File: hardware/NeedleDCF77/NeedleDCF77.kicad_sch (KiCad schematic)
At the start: 84 parts, among them J1 USB_C_Receptacle_USB2.0, J2 Battery, J3 DSW, J4 UART, J5 Hours, J6 Minutes, J7 Seconds, Q1 AO3401A, Q2 AO3400A, SW1 ShowDate, U1 LTC3558, U2 STM32L051C8Tx, U3 MAS6180_77kHz, U4 LT1617, U5 PT6312, U6 LM4871, Y2 32.768kHz

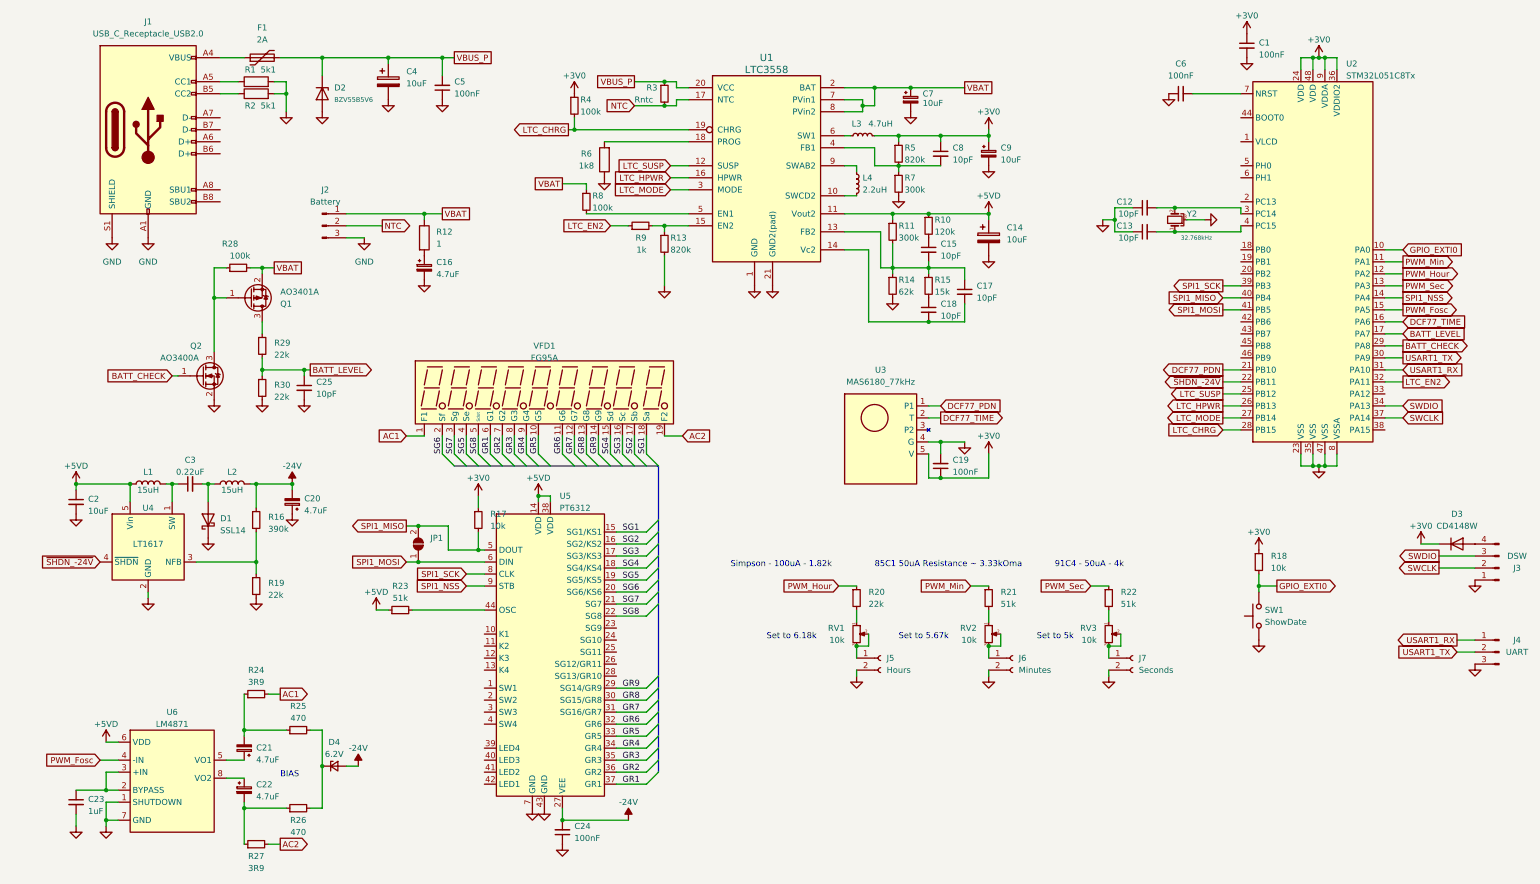
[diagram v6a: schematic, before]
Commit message: Initial version of PCB placement and routing
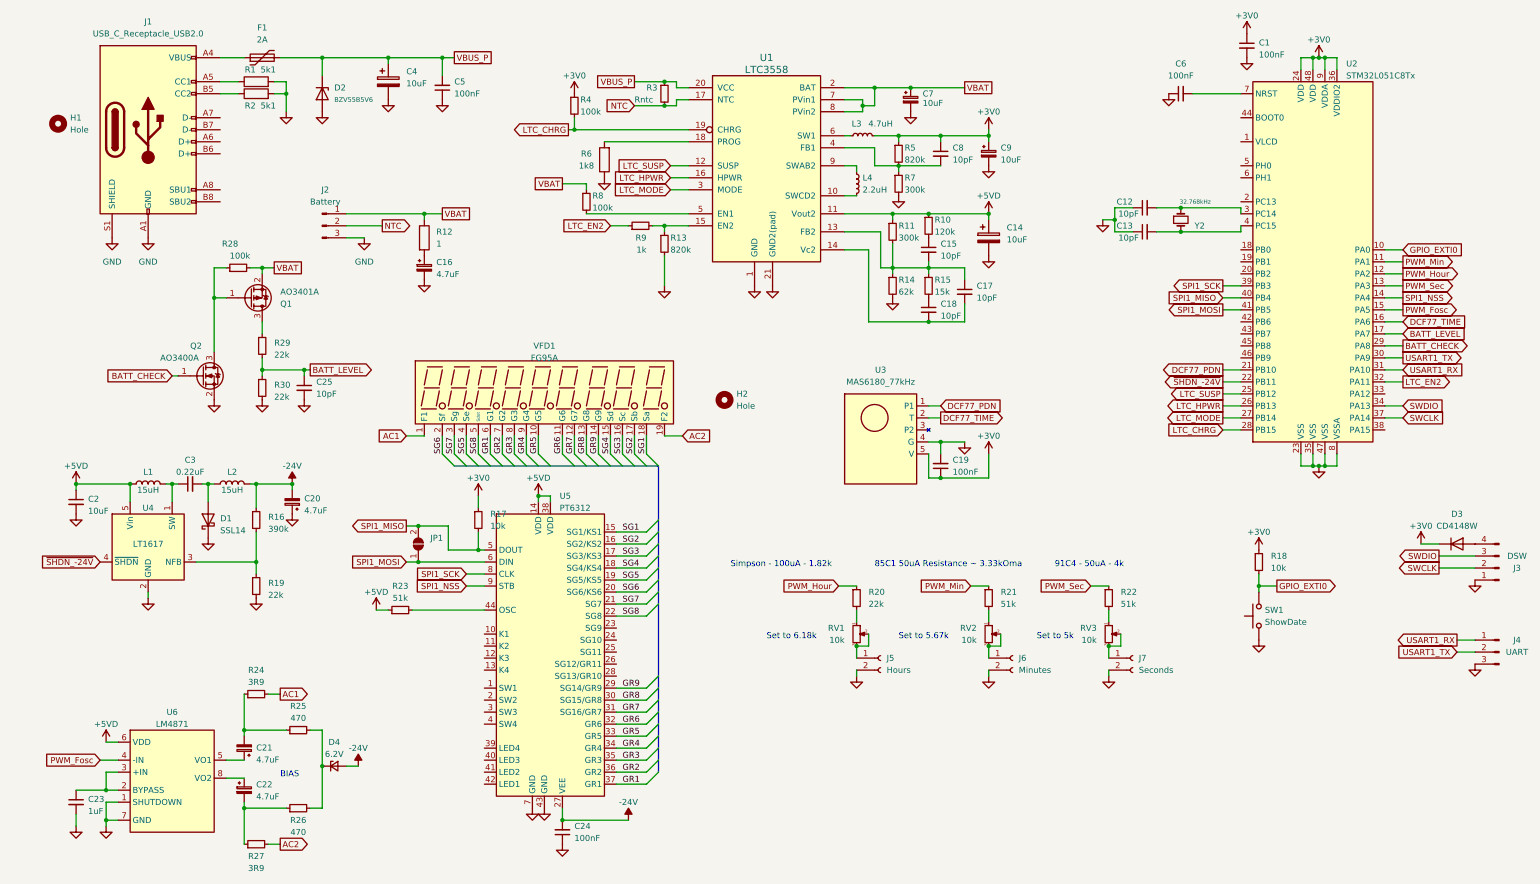
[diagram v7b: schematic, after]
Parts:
- added H1, H2: Hole, MountingHole:MountingHole_3.2mm_M3_DIN965_Pad_TopBottom, symbol Mechanical:MountingHole
- J1: footprint Connector_USB:USB_C_Receptacle_HRO_TYPE-C-31-M-12 -> Molex USB C:Molex-2169890001-MFG; Alie TYPE-C-31-M-12 -> 2169890001
- Y2: footprint Crystal:Crystal_C38-LF_D3.0mm_L8.0mm_Horizontal_1EP_style2 -> Crystal:Crystal_C38-LF_D3.0mm_L8.0mm_Horizontal; symbol Device:Crystal_GND3_Small -> Device:Crystal_Small
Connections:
- net GND: no longer Y2.3
- net at C13.2, U2.4 (PC15): now also Y2.2; no longer Y2.1
- net at C12.2, U2.3 (PC14): now also Y2.1; no longer Y2.2
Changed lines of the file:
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@@
   (junction (at 195.58 71.12) (diameter 0) (color 0 0 0 0)
   )
+  (junction (at 256.54 63.5) (diameter 0) (color 0 0 0 0)
+  )
   (junction (at 68.58 116.84) (diameter 0) (color 0 0 0 0)
   )
@@
   (junction (at 241.3 151.13) (diameter 0) (color 0 0 0 0)
   )
-  (junction (at 255.27 63.5) (diameter 0) (color 0 0 0 0)
-  )
   (junction (at 205.74 115.57) (diameter 0) (color 0 0 0 0)
   )
   (junction (at 205.74 43.18) (diameter 0) (color 0 0 0 0)
   )
+  (junction (at 256.54 58.42) (diameter 0) (color 0 0 0 0)
+  )
   (junction (at 60.96 116.84) (diameter 0) (color 0 0 0 0)
   )
   (junction (at 242.57 60.96) (diameter 0) (color 0 0 0 0)
   )
-  (junction (at 255.27 58.42) (diameter 0) (color 0 0 0 0)
-  )
   (junction (at 95.25 125.73) (diameter 0) (color 0 0 0 0)
   )
@@
     (stroke (width 0) (type default))
   )
-  (wire (pts (xy 251.46 63.5) (xy 255.27 63.5))
-    (stroke (width 0) (type default))
-  )
   (wire (pts (xy 241.3 156.21) (xy 241.3 157.48))
     (stroke (width 0) (type default))
@@
     (stroke (width 0) (type default))
   )
-  (wire (pts (xy 251.46 58.42) (xy 255.27 58.42))
-    (stroke (width 0) (type default))
-  )
   (bus (pts (xy 146.05 170.18) (xy 146.05 172.72))
     (stroke (width 0) (type default))
@@
     (stroke (width 0) (type default))
   )
-  (wire (pts (xy 255.27 58.42) (xy 269.24 58.42))
+  (wire (pts (xy 251.46 58.42) (xy 256.54 58.42))
     (stroke (width 0) (type default))
   )
@@
     (stroke (width 0) (type default))
   )
-  (wire (pts (xy 255.27 63.5) (xy 269.24 63.5))
+  (wire (pts (xy 251.46 63.5) (xy 256.54 63.5))
     (stroke (width 0) (type default))
   )
@@
     (stroke (width 0) (type default))
   )
-  (wire (pts (xy 257.81 60.96) (xy 261.62 60.96))
-    (stroke (width 0) (type default))
-  )
   (bus (pts (xy 146.05 165.1) (xy 146.05 167.64))
     (stroke (width 0) (type default))
@@
     (stroke (width 0) (type default))
   )
+  (wire (pts (xy 256.54 63.5) (xy 269.24 63.5))
+    (stroke (width 0) (type default))
+  )
   (wire (pts (xy 137.16 175.26) (xy 143.51 175.26))
     (stroke (width 0) (type default))
@@
     (stroke (width 0) (type default))
   )
+  (wire (pts (xy 256.54 58.42) (xy 269.24 58.42))
+    (stroke (width 0) (type default))
+  )
   (text "91C4 - 50uA - 4k" (at 229.87 134.62 0)
     (effects (font (size 1.27 1.27)) (justify left bottom))
@@
       (effects (font (size 1.27 1.27)))
     )
-    (property "Footprint" "Connector_USB:USB_C_Receptacle_HRO_TYPE-C-31-M-12" (at 41.91 41.91 0)
+    (property "Footprint" "Molex USB C:Molex-2169890001-MFG" (at 41.91 41.91 0)
       (effects (font (size 1.27 1.27)) hide)
     )
-    (property "Datasheet" "https://www.usb.org/sites/default/files/documents/usb_type-c.zip" (at 41.91 41.91 0)
+    (property "Datasheet" "https://www.molex.com/content/dam/molex/molex-dot-com/products/automated/en-us/salesdrawingpdf/216/216989/2169890001_sd.pdf?inline" (at 41.91 41.91 0)
       (effects (font (size 1.27 1.27)) hide)
     )
-    (property "Alie" "TYPE-C-31-M-12" (at 38.1 41.91 0)
+    (property "Alie" "2169890001" (at 38.1 41.91 0)
       (effects (font (size 1.27 1.27)) hide)
     )
@@
     )
   )
+  (symbol (lib_id "Mechanical:MountingHole") (at 19.05 40.64 0) (unit 1)
+    (in_bom yes) (on_board yes) (dnp no) (fields_autoplaced)
+    (property "Reference" "H1" (at 21.59 39.37 0)
+      (effects (font (size 1.27 1.27)) (justify left))
+    )
+    (property "Value" "Hole" (at 21.59 41.91 0)
+      (effects (font (size 1.27 1.27)) (justify left))
+    )
+    (property "Footprint" "MountingHole:MountingHole_3.2mm_M3_DIN965_Pad_TopBottom" (at 19.05 40.64 0)
+      (effects (font (size 1.27 1.27)) hide)
+    )
+    (property "Datasheet" "~" (at 19.05 40.64 0)
+      (effects (font (size 1.27 1.27)) hide)
+    )
+    (property "Kelco" "#8282" (at 19.05 40.64 0)
+      (effects (font (size 1.27 1.27)) hide)
+    )
+    (instances
+      (project "NeedleDCF77"
+        (path "/9538e4ed-27e6-4c37-b989-9859dc0d49e8"
+          (reference "H1") (unit 1)
+        )
+      )
+    )
+  )
   (symbol (lib_id "Device:R_Small") (at 62.23 87.63 0) (unit 1)
     (in_bom yes) (on_board yes) (dnp no) (fields_autoplaced)
@@
     )
   )
-  (symbol (lib_id "Device:Crystal_GND3_Small") (at 255.27 60.96 90) (unit 1)
+  (symbol (lib_id "Device:Crystal_Small") (at 256.54 60.96 270) (unit 1)
     (in_bom yes) (on_board yes) (dnp no)
-    (property "Reference" "Y2" (at 257.81 59.6899 90)
+    (property "Reference" "Y2" (at 261.62 62.23 90)
       (effects (font (size 1.27 1.27)) (justify right))
     )
-    (property "Value" "32.768kHz" (at 256.54 64.77 90)
+    (property "Value" "32.768kHz" (at 262.89 57.15 90)
       (effects (font (size 0.9 0.9)) (justify right))
     )
-    (property "Footprint" "Crystal:Crystal_C38-LF_D3.0mm_L8.0mm_Horizontal_1EP_style2" (at 255.27 60.96 0)
+    (property "Footprint" "Crystal:Crystal_C38-LF_D3.0mm_L8.0mm_Horizontal" (at 256.54 60.96 0)
       (effects (font (size 1.27 1.27)) hide)
     )
-    (property "Datasheet" "~" (at 255.27 60.96 0)
+    (property "Datasheet" "~" (at 256.54 60.96 0)
       (effects (font (size 1.27 1.27)) hide)
     )
-    (property "Kelco" "#13076" (at 255.27 60.96 90)
+    (property "Kelco" "#13076" (at 256.54 60.96 90)
       (effects (font (size 1.27 1.27)) hide)
     )
     (pin "1")
     (pin "2")
-    (pin "3")
     (instances
       (project "NeedleDCF77"
@@
     )
   )
+  (symbol (lib_id "Mechanical:MountingHole") (at 160.02 99.06 0) (unit 1)
+    (in_bom yes) (on_board yes) (dnp no) (fields_autoplaced)
+    (property "Reference" "H2" (at 162.56 97.79 0)
+      (effects (font (size 1.27 1.27)) (justify left))
+    )
+    (property "Value" "Hole" (at 162.56 100.33 0)
+      (effects (font (size 1.27 1.27)) (justify left))
+    )
+    (property "Footprint" "MountingHole:MountingHole_3.2mm_M3_DIN965_Pad_TopBottom" (at 160.02 99.06 0)
+      (effects (font (size 1.27 1.27)) hide)
+    )
+    (property "Datasheet" "~" (at 160.02 99.06 0)
+      (effects (font (size 1.27 1.27)) hide)
+    )
+    (property "Kelco" "#8282" (at 160.02 99.06 0)
+      (effects (font (size 1.27 1.27)) hide)
+    )
+    (instances
+      (project "NeedleDCF77"
+        (path "/9538e4ed-27e6-4c37-b989-9859dc0d49e8"
+          (reference "H2") (unit 1)
+        )
+      )
+    )
+  )
   (symbol (lib_id "Transistor_FET:AO3401A") (at 59.69 77.47 0) (mirror x) (unit 1)
     (in_bom yes) (on_board yes) (dnp no)
@@
         )
       )
-    )
-  )
-  (symbol (lib_id "power:GND") (at 261.62 60.96 90) (unit 1)
-    (in_bom yes) (on_board yes) (dnp no) (fields_autoplaced)
-    (property "Reference" "#PWR031" (at 267.97 60.96 0)
-      (effects (font (size 1.27 1.27)) hide)
-    )
-    (property "Value" "GND" (at 266.7 60.96 0)
-      (effects (font (size 1.27 1.27)) hide)
-    )
-    (property "Footprint" "" (at 261.62 60.96 0)
-      (effects (font (size 1.27 1.27)) hide)
-    )
-    (property "Datasheet" "" (at 261.62 60.96 0)
-      (effects (font (size 1.27 1.27)) hide)
-    )
-    (pin "1")
-    (instances
-      (project "NeedleDCF77"
-        (path "/9538e4ed-27e6-4c37-b989-9859dc0d49e8"
-          (reference "#PWR031") (unit 1)
-        )
-      )

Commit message: Add test points to schematic and board
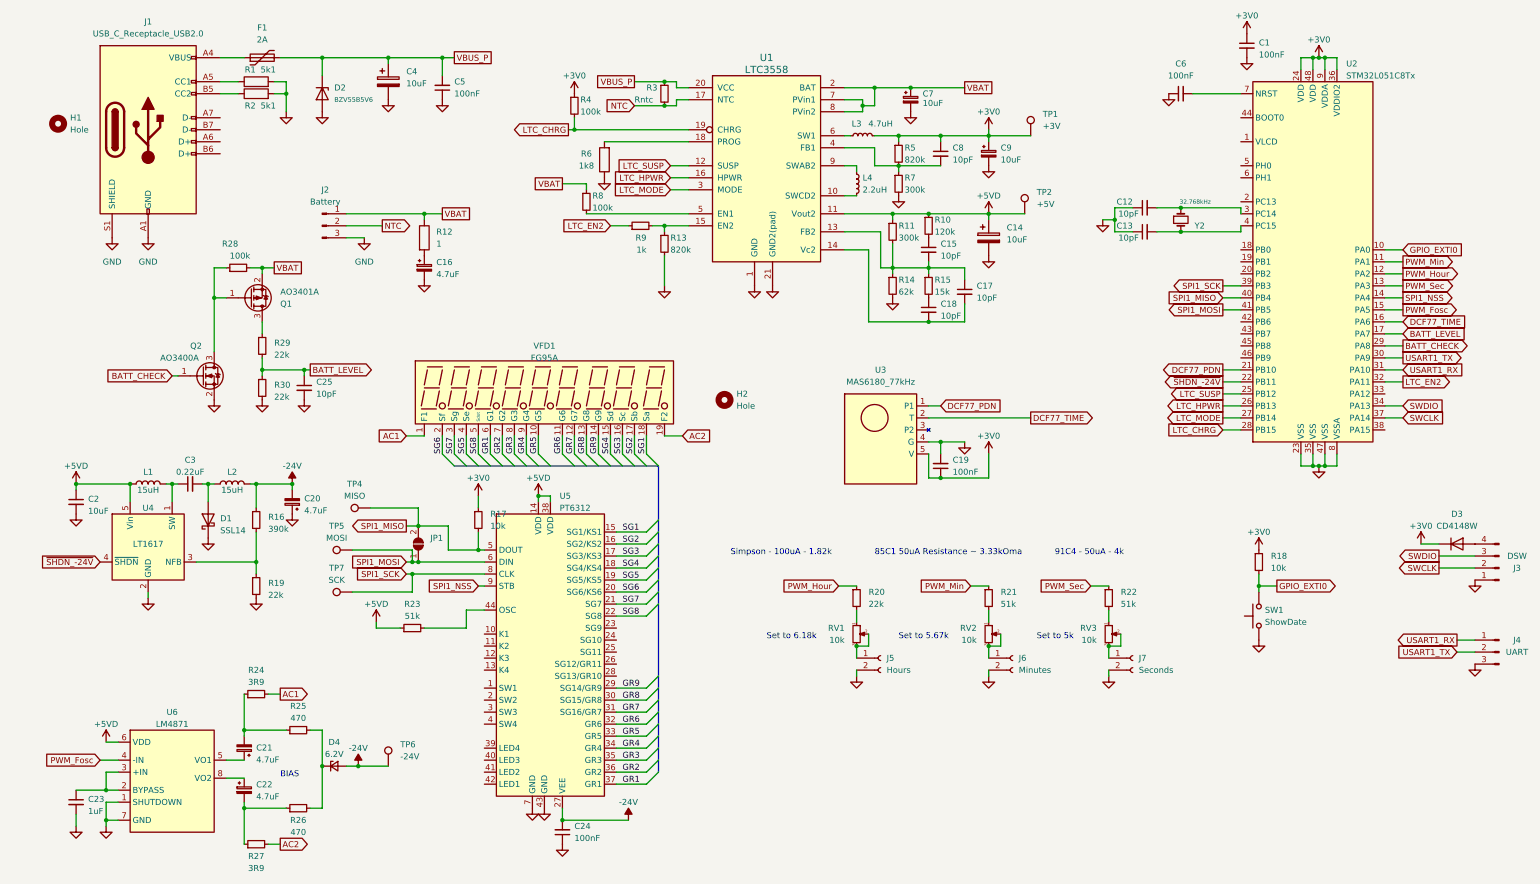
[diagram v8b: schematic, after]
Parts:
- added TP1: +3V, TestPoint:TestPoint_Pad_1.5x1.5mm, symbol Connector:TestPoint
- added TP2: +5V, TestPoint:TestPoint_Pad_1.5x1.5mm, symbol Connector:TestPoint
- added TP4: MISO, TestPoint:TestPoint_Pad_1.5x1.5mm, symbol Connector:TestPoint
- added TP5: MOSI, TestPoint:TestPoint_Pad_1.5x1.5mm, symbol Connector:TestPoint
- added TP6: -24V, TestPoint:TestPoint_Pad_1.5x1.5mm, symbol Connector:TestPoint
- added TP7: SCK, TestPoint:TestPoint_Pad_1.5x1.5mm, symbol Connector:TestPoint
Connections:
- net +3V0: now also TP1.1
- net +5VD: now also TP2.1
- net -24V: now also TP6.1
- net SPI1_MISO: now also TP4.1
- net SPI1_MOSI: now also TP5.1
- net SPI1_SCK: now also TP7.1
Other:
- moved on the sheet: R23
